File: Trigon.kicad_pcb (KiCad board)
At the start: 2 copper layers, 160 x 120 mm, 72 parts, among them J1 USB_C_Receptacle_USB2.0, SW1 SW_Push, SW2 Rotary_Encoder_Switch, U1 ATmega32U4-AU, Y1 16MHz

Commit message: new usb connector'
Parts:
- F1: value Polyfuse_Small -> 500mA
- J1: value USB_C_Receptacle_USB2.0 -> TYPE-C-31-M12_13; footprint Connector_USB:USB_C_Receptacle_Palconn_UTC16-G -> acheron_Connectors:TYPE-C-31-M-12
- moved G*** 19.8 mm to (78.6, -55.6)
- moved R1 12.0 mm to (77.2, -105.3)
- moved R2 12.0 mm to (75.2, -105.3)
- moved R5 3.31 mm to (79.2, -105.3), turned to 90 degrees
- moved J1 3.30 mm to (76.2, -108.0)
- moved F1 2.90 mm to (85.6, -104.8), turned to 90 degrees
- moved R4 2.16 mm to (73.2, -105.3), turned to 90 degrees
- moved G*** 1.77 mm to (79.4, -34.9)
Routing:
- net D+: track 18.1 -> 4.94 mm
- net Net-(R2-Pad1): track 73.8 -> 85.6 mm
- net Net-(R1-Pad1): track 72.4 -> 83.9 mm
- net D-: track 17.5 -> 7.03 mm
- net Net-(J1-PadB5): track 9.38 -> 3.54 mm, vias 2 -> 0
- net Net-(D4-Pad2): track 10.2 -> 12.5 mm
- net +5V: track 158.3 -> 156.2 mm
- net Net-(J1-PadA5): track 5.01 -> 3.83 mm
- net VCC: track 14.6 -> 15.2 mm

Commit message: latest
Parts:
- moved G*** 128.6 mm to (92.6, 72.3), turned to 180 degrees
- moved C1 128.5 mm to (152.7, 43.2)
- moved C4 128.5 mm to (155.6, 48.4)
- moved C5 128.5 mm to (150.8, 62.7)
- moved C6 128.5 mm to (142.4, 44.2)
- moved D1 128.5 mm to (42.1, 35.7)
- moved D10 128.5 mm to (80.2, 54.8)
- moved D11 128.5 mm to (99.2, 54.8)
- moved D12 128.5 mm to (117.5, 54.8)
- moved D13 128.5 mm to (136.5, 55.0)
- moved D19 128.5 mm to (42.1, 92.9)
- moved D2 128.5 mm to (61.1, 35.7)
- moved D20 128.5 mm to (61.1, 92.9)
- moved D21 128.5 mm to (80.2, 92.9)
- moved D22 128.5 mm to (99.2, 92.9)
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
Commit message: Checkpoint
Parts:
- removed the G*** at (92.6, 72.3)
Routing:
- net Net-(R1-Pad1): track 83.9 -> 82.5 mm
- net Net-(R2-Pad1): track 85.6 -> 84.3 mm
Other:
- outline, holes or cut-outs redrawn

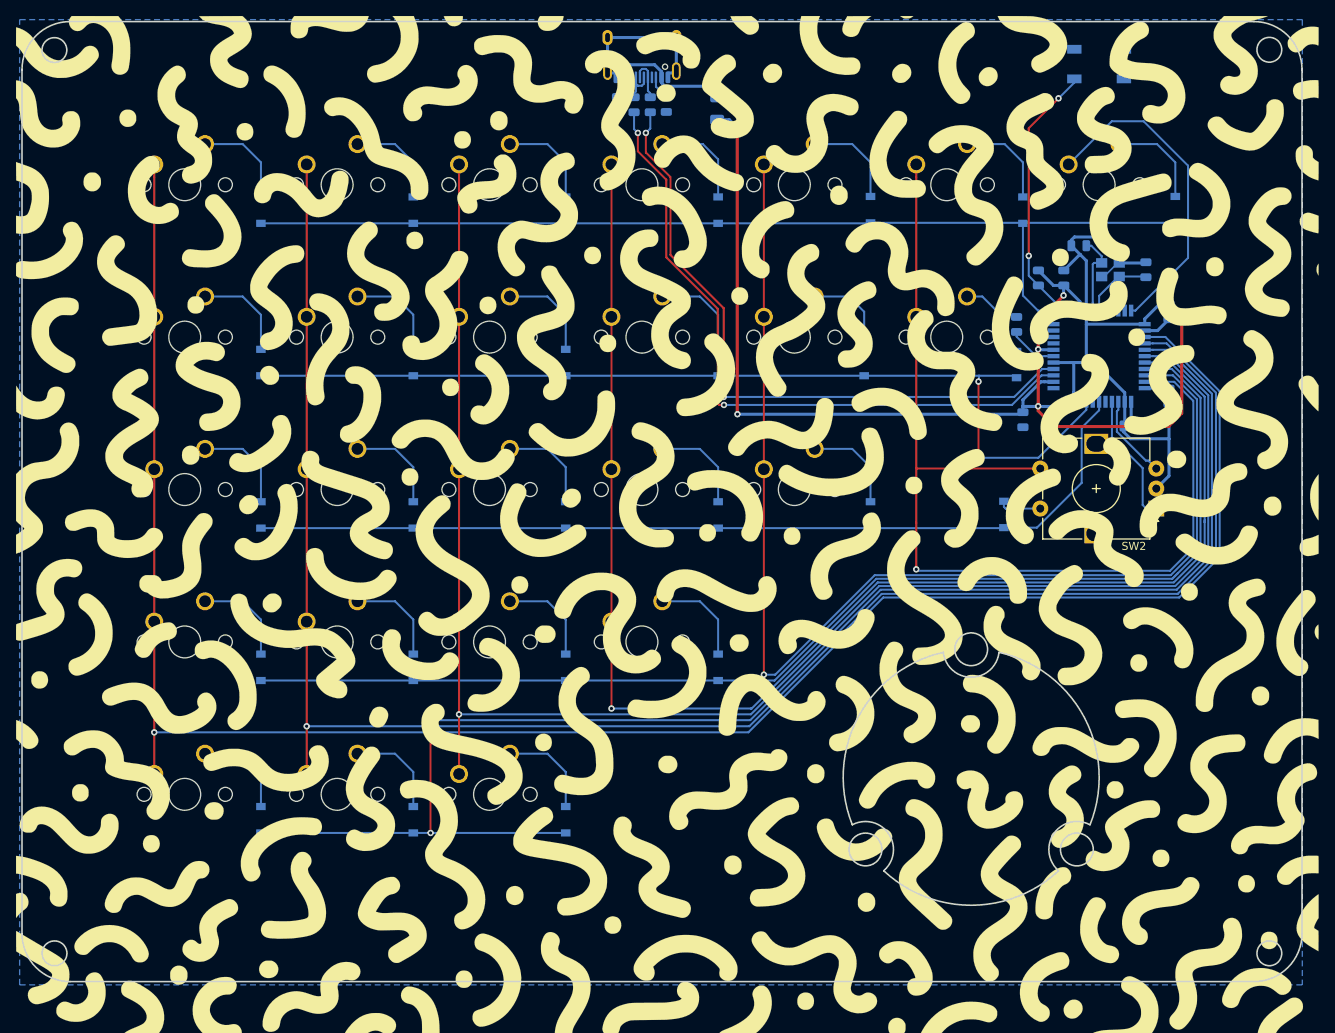
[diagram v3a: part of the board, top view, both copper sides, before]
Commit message: usb hub pcb layout
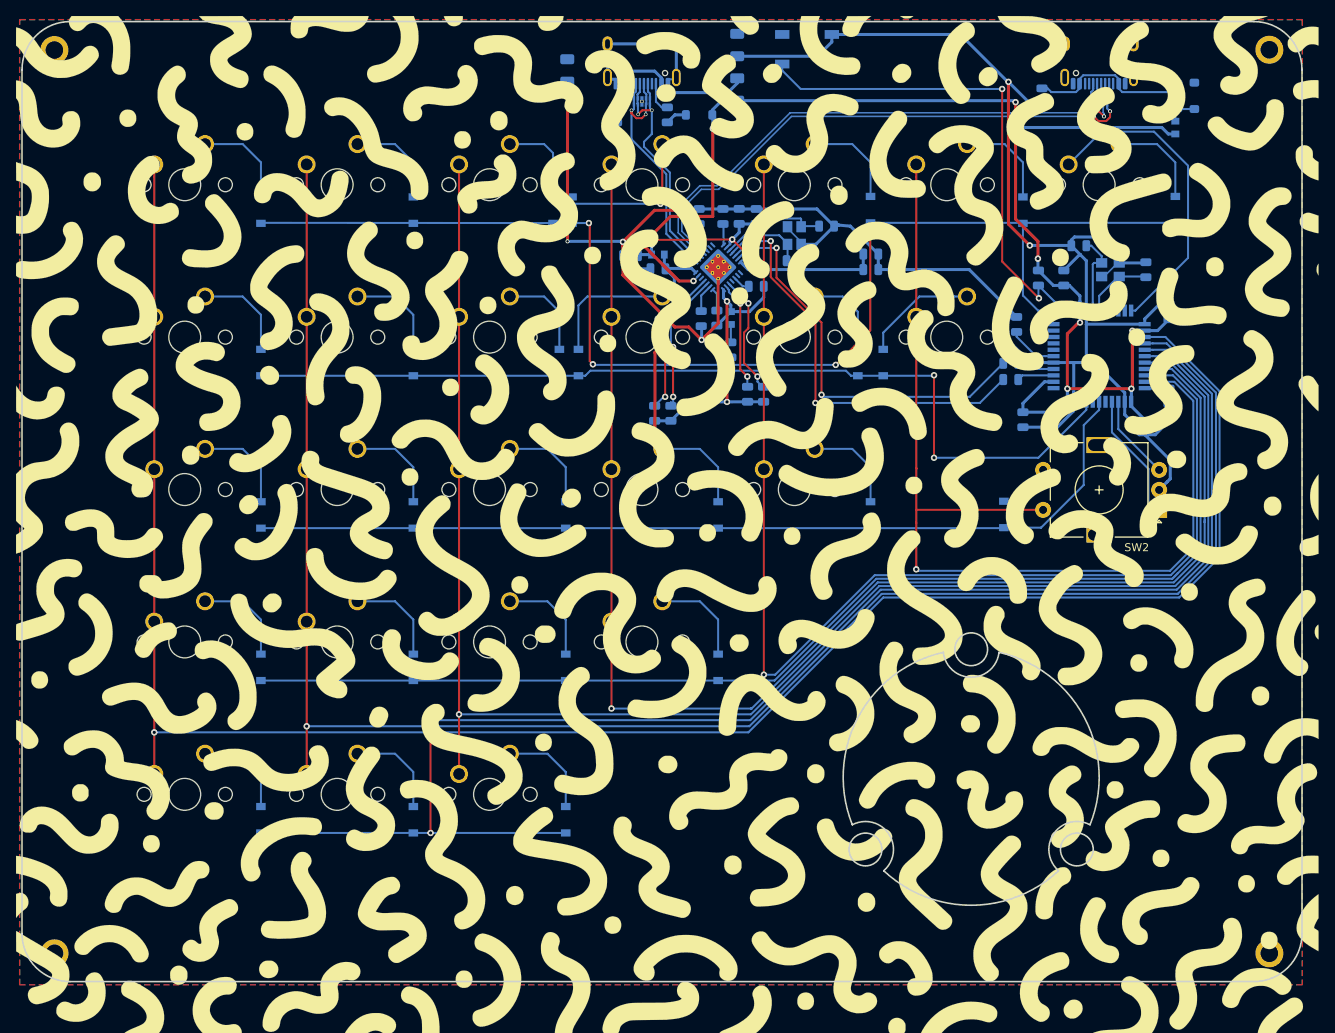
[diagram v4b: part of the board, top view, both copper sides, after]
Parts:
- added C10: 22pF, Capacitor_SMD:C_0805_2012Metric, B.Cu at (108.7, 42.0)
- added C11: 10uF, Capacitor_SMD:C_0805_2012Metric, B.Cu at (91.7, 43.1)
- added C12: 0.1uF, Capacitor_SMD:C_0805_2012Metric, B.Cu at (88.3, 41.4)
- added C13: 0.1uF, Capacitor_SMD:C_0805_2012Metric, B.Cu at (96.8, 36.5)
- added C14: 0.1uF, Capacitor_SMD:C_0805_2012Metric, B.Cu at (101.9, 36.5)
- added C15: 1uF, Capacitor_SMD:C_0805_2012Metric, B.Cu at (104.0, 36.5)
- added C16: 1uF, Capacitor_SMD:C_0805_2012Metric, B.Cu at (118.3, 43.1)
- added C17: 0.1uF, Capacitor_SMD:C_0805_2012Metric, B.Cu at (118.3, 41.2)
- added C18: 0.1uF, Capacitor_SMD:C_0805_2012Metric, B.Cu at (139.7, 21.4)
- added C8: 0.1uF, Capacitor_SMD:C_0805_2012Metric, B.Cu at (100.8, 53.2)
- added C9: 22pF, Capacitor_SMD:C_0805_2012Metric, B.Cu at (112.8, 37.7)
- added D27: 9V Breakdown, acheron_Components:D_SOD-123_Bidirectional, B.Cu at (96.8, 23.8)
- added D28: 9V Breakdown, acheron_Components:D_SOD-123_Bidirectional, B.Cu at (158.8, 21.4)
- added F2: 500mA, Fuse:Fuse_1206_3216Metric, B.Cu at (156.4, 21.4)
- added FB1: 600R, josh-passives-smt:Ferrite_Bead_0603, B.Cu at (100.8, 49.2)
- added FB2: 600R, josh-passives-smt:Ferrite_Bead_0603, B.Cu at (91.7, 41.3)
- added FB3: 600R, josh-passives-smt:Ferrite_Bead_0603, B.Cu at (156.4, 25.4)
- added J2: TYPE-C-31-M12_13, acheron_Connectors:TYPE-C-31-M-12, B.Cu at (146.8, 20.6)
- added L1: L_Core_Ferrite, Inductor_SMD:L_1206_3216Metric, B.Cu at (101.6, 15.1)
- added L2: L_Core_Ferrite, Inductor_SMD:L_1206_3216Metric, B.Cu at (80.4, 18.3)
- added MH1: Mount-M2, random-keyboard-parts:Generic-Mounthole, F.Cu at (16.3, 128.6)
- added MH2: Mount-M2, random-keyboard-parts:Generic-Mounthole, F.Cu at (168.1, 15.7)
- added MH3: Mount-M2, random-keyboard-parts:Generic-Mounthole, F.Cu at (168.1, 128.6)
- added MH4: Mount-M2, random-keyboard-parts:Generic-Mounthole, F.Cu at (16.3, 15.7)
- added R10: 650R, Resistor_SMD:R_0805_2012Metric, B.Cu at (99.8, 36.5)
- added R11: 10k, Resistor_SMD:R_0805_2012Metric, B.Cu at (91.3, 61.1)
- added R12: 10k, Resistor_SMD:R_0805_2012Metric, B.Cu at (93.3, 61.1)
- added R13: 10k, Resistor_SMD:R_0805_2012Metric, B.Cu at (102.9, 58.7)
- added R14: 10k, Resistor_SMD:R_0805_2012Metric, B.Cu at (104.9, 58.7)
- added R7: 100k, Resistor_SMD:R_0805_2012Metric, B.Cu at (99.1, 49.2)
- added R8: 100k, Resistor_SMD:R_0805_2012Metric, B.Cu at (97.1, 49.3)
- added R9: 10k, Resistor_SMD:R_0805_2012Metric, B.Cu at (104.0, 45.2)
- added U2: TPD4E05U06DQAR, Package_SON:USON-10_2.5x1.0mm_P0.5mm, B.Cu at (89.7, 22.1)
- added U3: CY7C65632-28LTXCT, Package_DFN_QFN:QFN-28-1EP_5x5mm_P0.5mm_EP3.35x3.35mm_ThermalVias, B.Cu at (99.2, 42.9)
- added U4: TPD4E05U06DQAR, Package_SON:USON-10_2.5x1.0mm_P0.5mm, B.Cu at (146.8, 22.2)
- added Y2: 12MHz, Crystal:Crystal_SMD_3225-4Pin_3.2x2.5mm, B.Cu at (108.7, 38.9)
- SW2: footprint Rotary_Encoder:RotaryEncoder_Alps_EC12E-Switch_Vertical_H20mm -> Keebio-Parts:RotaryEncoder_Alps_EC11E-Switch_Vertical_H20mm
- moved R2 58.3 mm to (135.8, 56.9), turned to 180 degrees
- moved R1 55.4 mm to (135.8, 54.9), turned to 180 degrees
- moved SW1 36.6 mm to (110.3, 15.6)
- moved D4 18.3 mm to (81.0, 35.7)
- moved D11 17.5 mm to (81.8, 54.8)
- moved D13 16.7 mm to (119.9, 54.8)
- moved SW2 7.52 mm to (146.8, 70.7)
- moved F1 3.46 mm to (101.6, 20.6)
- moved C5 1.59 mm to (152.4, 62.7)
- moved D3 1.59 mm to (78.6, 35.7)
- moved R4 1.31 mm to (86.5, 23.8)
- moved R5 1.31 mm to (92.9, 23.8)
- moved D10 0.79 mm to (79.4, 54.8)
- moved J1 0.79 mm to (89.7, 20.6)
- moved D12 0.79 mm to (116.7, 54.8)
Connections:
- net VCC renamed Net-(F1-Pad2)
- J1 pad A1: GND -> GNDPWR
- J1 pad A6: D+ -> DA+
- J1 pad A7: D- -> DA-
- J1 pad B1: GND -> GNDPWR
- J1 pad B6: D+ -> DA+
- J1 pad B7: D- -> DA-
- J1 pad S: GND -> GNDPWR
- R1 pad 2: D+ -> D3_D+
- R2 pad 2: D- -> D3_D-
- R4 pad 1: GND -> GNDPWR
- R5 pad 1: GND -> GNDPWR
- U1 pad 7: +5V -> VBUS
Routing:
- net GND: track 102.0 -> 307.3 mm, vias 0 -> 7
- net Net-(R2-Pad1): track 84.3 -> 4.63 mm, vias 2 -> 0
- net Net-(R1-Pad1): track 82.5 -> 4.71 mm, vias 2 -> 0
- net D1A_D-: track 0.00 -> 77.3 mm, vias 0 -> 2
- net D1A_D+: track 0.00 -> 76.4 mm, vias 0 -> 2
- net VREG_3V3: track 0.00 -> 68.1 mm, vias 0 -> 4
- net D3_D-: track 0.00 -> 52.9 mm, vias 0 -> 2
- net D3_D+: track 0.00 -> 50.7 mm, vias 0 -> 2
- net +3.3VA: track 0.00 -> 46.1 mm, vias 0 -> 4
- net DA-: track 0.00 -> 34.5 mm, vias 0 -> 2
- net DA+: track 0.00 -> 33.1 mm, vias 0 -> 2
- net ROW0: track 129.7 -> 162.3 mm, vias 0 -> 4
- net Net-(R3-Pad2): track 35.0 -> 65.2 mm
- net GNDPWR: track 0.00 -> 23.8 mm, vias 0 -> 2
- net Net-(C18-Pad1): track 0.00 -> 20.8 mm
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- added copper zone on B.Cu, net GNDPWR
- added copper zone on F.Cu, net GNDPWR
- removed copper zone on B.Cu, net GND
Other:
- outline, holes or cut-outs redrawn
- net class Narrow added: clearance 0.127, trace_width 0.254, via_dia 0.8, via_drill 0.4
- rule trace_min: 0.2 -> 0.1524
- board text added: "rev 0.1"
- board text removed: "rev 0"

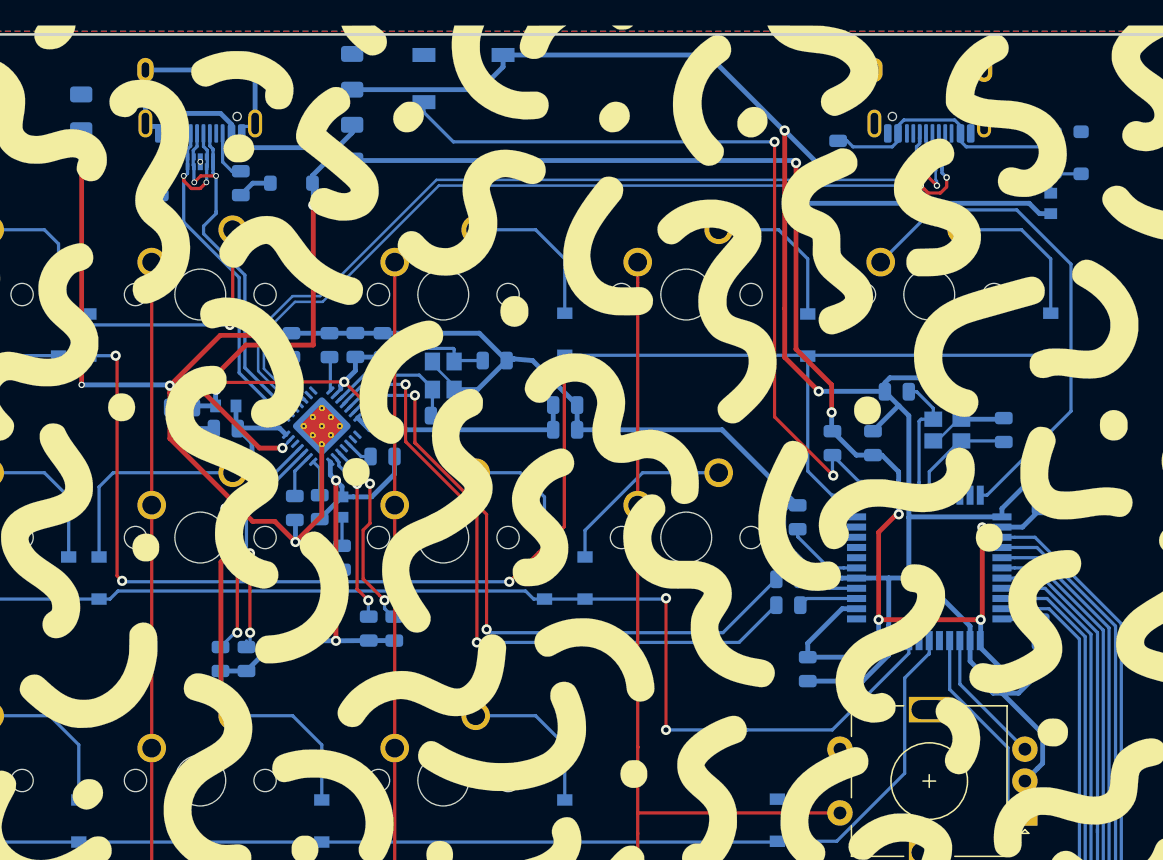
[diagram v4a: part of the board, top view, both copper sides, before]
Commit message: More compact layout
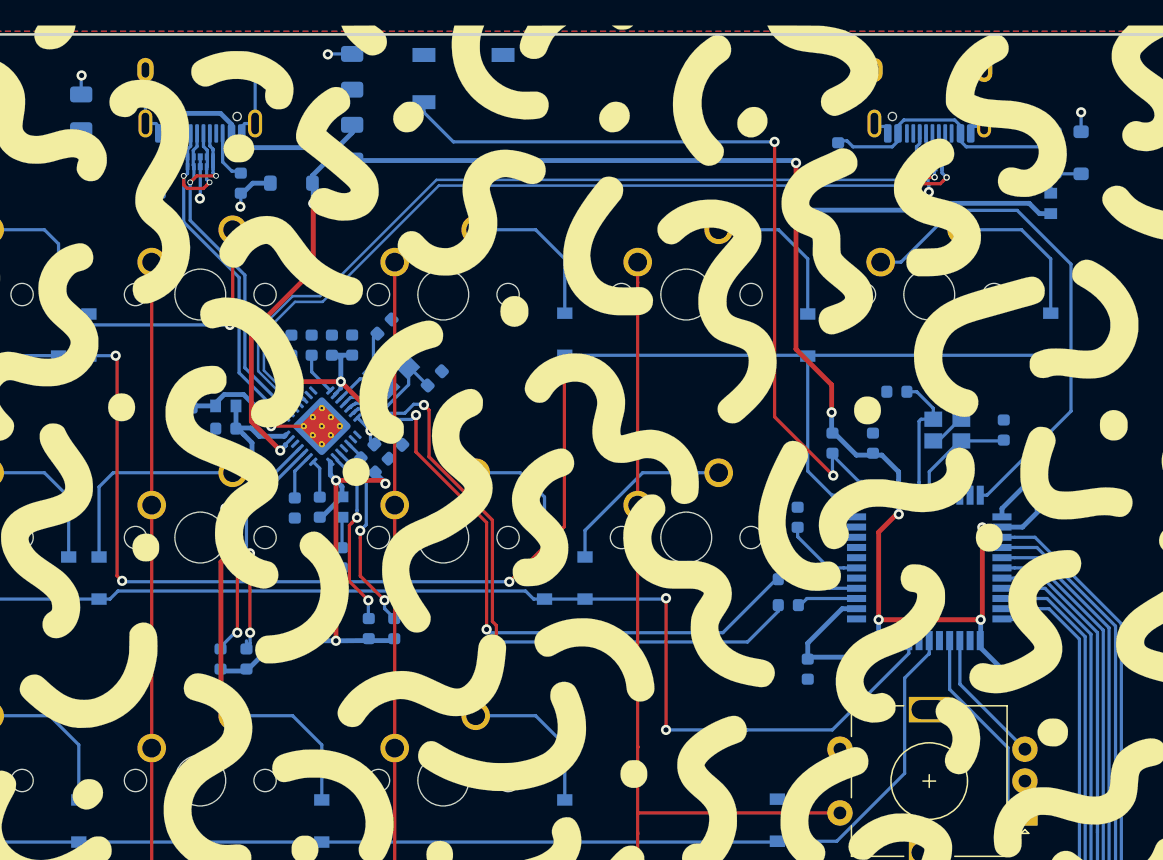
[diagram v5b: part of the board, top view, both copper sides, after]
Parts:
- C1, C10, C11, C12, C13, C14, C15, C16, C17, C18, C2, C3, C4, C5, C6, C7, C8, C9: footprint Capacitor_SMD:C_0805_2012Metric -> Capacitor_SMD:C_0603_1608Metric
- D27, D28: value 9V Breakdown -> 6V Breakdown
- F2: value 500mA -> 200mA
- L1, L2: value L_Core_Ferrite -> 60R@100MHz
- R1, R10, R11, R12, R13, R14, R2, R3, R4, R5, R6, R7, R8, R9: footprint Resistor_SMD:R_0805_2012Metric -> Resistor_SMD:R_0603_1608Metric
- moved C16 14.5 mm to (103.9, 44.9), turned to 315 degrees
- moved C17 13.6 mm to (105.0, 43.8), turned to 315 degrees
- moved C9 9.04 mm to (104.1, 35.1), turned to 45 degrees
- moved Y2 4.12 mm to (104.6, 38.5), turned to 45 degrees
- moved C10 2.99 mm to (108.1, 39.1), turned to 45 degrees
- moved C15 2.38 mm to (101.6, 36.5)
- moved C14 1.84 mm to (100.0, 36.5)
- moved R10 1.40 mm to (98.4, 36.5)
- moved R9 1.35 mm to (102.8, 45.9), turned to 135 degrees
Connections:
- MH1 pad 1: Net-(MH1-Pad1) -> GNDPWR
- MH3 pad 1: Net-(MH3-Pad1) -> GNDPWR
- MH4 pad 1: Net-(MH4-Pad1) -> GNDPWR
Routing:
- net GND: track 307.3 -> 14.2 mm, vias 7 -> 1
- net +3.3VA: track 46.1 -> 31.9 mm
- net Net-(C9-Pad1): track 13.9 -> 6.73 mm
- net +5V: track 172.9 -> 166.9 mm
- net GNDPWR: track 23.8 -> 28.9 mm, vias 2 -> 7
- net D3_D+: track 50.7 -> 49.2 mm
- net D3_D-: track 52.9 -> 51.5 mm
- net D1A_D-: track 77.3 -> 76.1 mm
- net VREG_3V3: track 68.1 -> 67.1 mm, vias 4 -> 5
- net Net-(C10-Pad1): track 10.5 -> 9.62 mm
- net Net-(R10-Pad1): track 2.82 -> 3.55 mm
- net D1A_D+: track 76.4 -> 75.7 mm
- net Net-(R9-Pad2): track 2.15 -> 1.53 mm
- net DA-: track 34.5 -> 35.0 mm
- added copper zone on B.Cu, net GND
- removed copper zone on B.Cu, net GNDPWR
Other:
- board text added: "rev 0"
- board text removed: "rev 0.1"

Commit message: incorporating josh's feedback
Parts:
- removed G***: LOGO, Trigon:wiggle
- removed L1, L2: 60R@100MHz, Inductor_SMD:L_1206_3216Metric
- added C19: 0.1uF, Capacitor_SMD:C_0603_1608Metric, B.Cu at (94.4, 18.3)
- added C20: 0.1uF, Capacitor_SMD:C_0603_1608Metric, B.Cu at (138.9, 18.3)
- added C21: 0.1uF, Capacitor_SMD:C_0603_1608Metric, B.Cu at (95.9, 23.2)
- added FB4: 600R, josh-passives-smt:Ferrite_Bead_0603, B.Cu at (95.9, 27.1)
- added R15: 100k, Resistor_SMD:R_0603_1608Metric, B.Cu at (92.8, 18.2)
- added R16: 100k, Resistor_SMD:R_0603_1608Metric, B.Cu at (140.5, 18.3)
- U2, U4: value TPD4E05U06DQAR -> USBLC6-2SC6; footprint Package_SON:USON-10_2.5x1.0mm_P0.5mm -> Package_TO_SOT_SMD:SOT-23-6
- moved R11 21.8 mm to (88.3, 39.5), turned to 0 degrees
- moved R12 20.7 mm to (88.3, 41.0), turned to 0 degrees
- moved D6 17.8 mm to (119.5, 35.7)
- moved SW1 17.6 mm to (127.8, 18.0)
- moved C18 13.1 mm to (152.7, 22.5), turned to 0 degrees
- moved R7 12.7 mm to (88.3, 42.5), turned to 180 degrees
- moved R10 12.7 mm to (110.7, 39.4)
- moved R14 12.1 mm to (100.6, 47.4)
- moved R13 11.9 mm to (99.1, 47.4)
- moved R4 11.7 mm to (98.2, 23.0)
- moved U2 11.1 mm to (100.7, 23.8), turned to 270 degrees
- moved J1 11.0 mm to (100.7, 20.6)
- moved R5 10.4 mm to (103.3, 23.0)
- moved D27 8.20 mm to (90.8, 18.3), turned to 90 degrees
- moved F1 7.92 mm to (95.1, 25.1), turned to 0 degrees
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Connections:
- C8 pad 1: Net-(C8-Pad1) -> VREG_3V3
- D27 pad 1: +5V -> Net-(D27-Pad1)
- D27 pad 2: GNDPWR -> GND
- D28 pad 2: GNDPWR -> GND
- F1 pad 1: +5V -> Net-(D27-Pad1)
- F1 pad 2: Net-(F1-Pad2) -> VBUS
- FB1 pad 1: VREG_3V3 -> Net-(FB1-Pad1)
- FB1 pad 2: Net-(C8-Pad1) -> VREG_3V3
- J1 pad A1: GNDPWR -> GND
- J1 pad A4: Net-(F1-Pad2) -> VBUS
- J1 pad A6: DA+ -> UP_DP
- J1 pad A7: DA- -> UP_DN
- J1 pad B1: GNDPWR -> GND
- J1 pad B4: Net-(F1-Pad2) -> VBUS
- J1 pad B6: DA+ -> UP_DP
- J1 pad B7: DA- -> UP_DN
- J1 pad S: GNDPWR -> Net-(C19-Pad1)
- J2 pad A1: GNDPWR -> GND
- J2 pad A6: D1A_D+ -> D1_DP
- J2 pad A7: D1A_D- -> D1_DN
- J2 pad B1: GNDPWR -> GND
- J2 pad B6: D1A_D+ -> D1_DP
- J2 pad B7: D1A_D- -> D1_DN
- J2 pad S: GNDPWR -> Net-(C20-Pad1)
- MH1 pad 1: GNDPWR -> GND
- MH2 pad 1: GNDPWR -> GND
- MH3 pad 1: GNDPWR -> GND
- MH4 pad 1: GNDPWR -> GND
- R4 pad 1: GNDPWR -> GND
- R5 pad 1: GNDPWR -> GND
- U1 pad 7: VBUS -> +5V
- U2 pad 1: DA+ -> UP_DN
- U2 pad 2: DA- -> GND
- U2 pad 3: GNDPWR -> UP_DP
- U2 pad 4: DA+ -> UP_D+
- U2 pad 5: DA- -> VBUS
- U2 pad 6: DA- -> UP_D-
- U3 pad 1: DA- -> UP_D-
- U3 pad 2: DA+ -> UP_D+
- U3 pad 21: VREG_3V3 -> Net-(FB1-Pad1)
- U3 pad 3: D1A_D- -> D1_D-
- U3 pad 4: D1A_D+ -> D1_D+
- U4 pad 1: D1A_D+ -> D1_DN
- U4 pad 2: D1A_D- -> GND
- U4 pad 3: GNDPWR -> D1_DP
- U4 pad 4: D1A_D+ -> D1_D+
- U4 pad 5: D1A_D- -> Net-(C18-Pad1)
- U4 pad 6: D1A_D- -> D1_D-
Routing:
- net D1A_D-: track 76.1 -> 0.00 mm, vias 2 -> 0
- net D1A_D+: track 75.7 -> 0.00 mm, vias 2 -> 0
- net +5V: track 166.9 -> 237.0 mm, vias 9 -> 10
- net D1_D+: track 0.00 -> 61.9 mm
- net D1_D-: track 0.00 -> 61.6 mm
- net DA-: track 35.0 -> 0.00 mm, vias 2 -> 0
- net DA+: track 33.0 -> 0.00 mm, vias 2 -> 0
- net VREG_3V3: track 67.1 -> 37.3 mm, vias 5 -> 0
- net GNDPWR: track 28.9 -> 0.00 mm, vias 7 -> 0
- net Net-(R3-Pad2): track 65.2 -> 93.4 mm
- net GND: track 14.2 -> 39.9 mm, vias 1 -> 28
- net +3.3VA: track 31.9 -> 54.7 mm, vias 4 -> 5
- net Net-(C19-Pad1): track 0.00 -> 20.7 mm
- net Net-(C20-Pad1): track 0.00 -> 20.6 mm
- net VBUS: track 0.00 -> 19.0 mm
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- added copper zone on F.Cu, net GND
- removed copper zone on F.Cu, net GNDPWR
